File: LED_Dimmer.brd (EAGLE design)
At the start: 48.3 x 62.2 mm, 12 parts

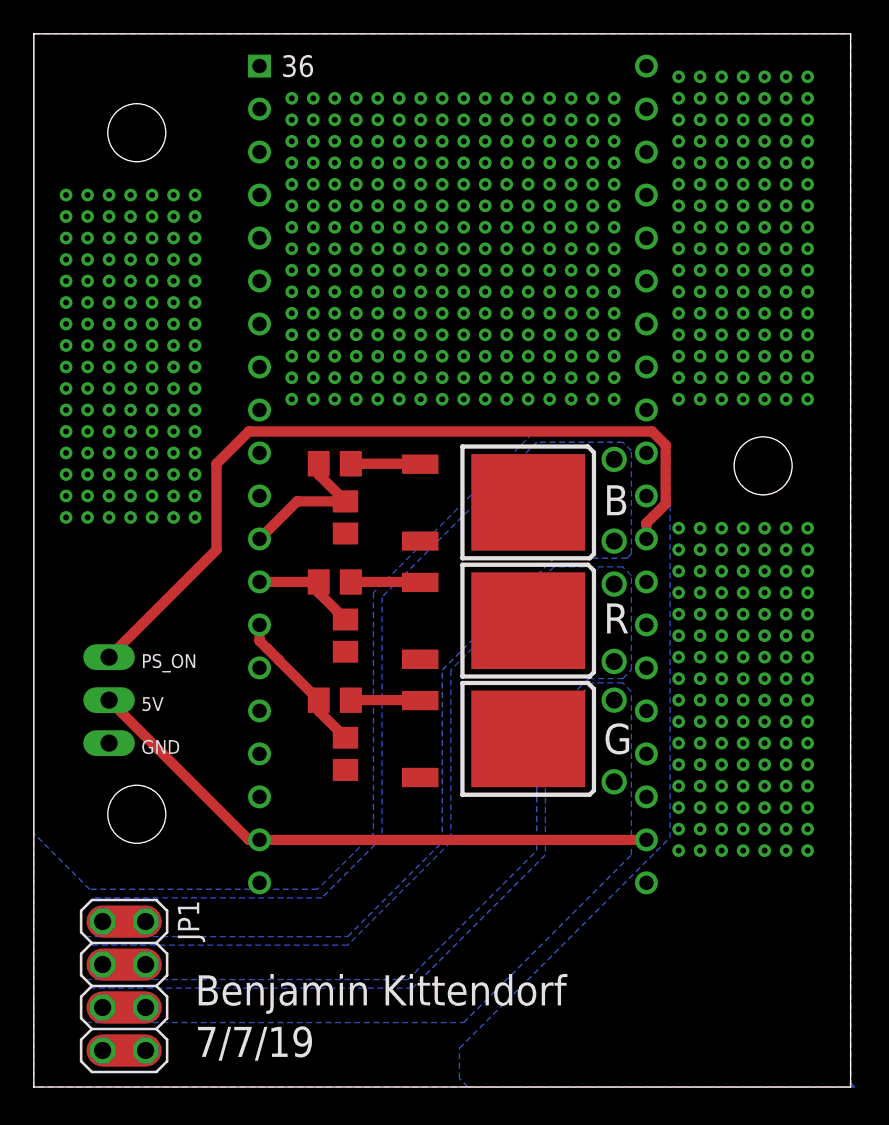
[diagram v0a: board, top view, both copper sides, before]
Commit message: retraced paths and edited clearances
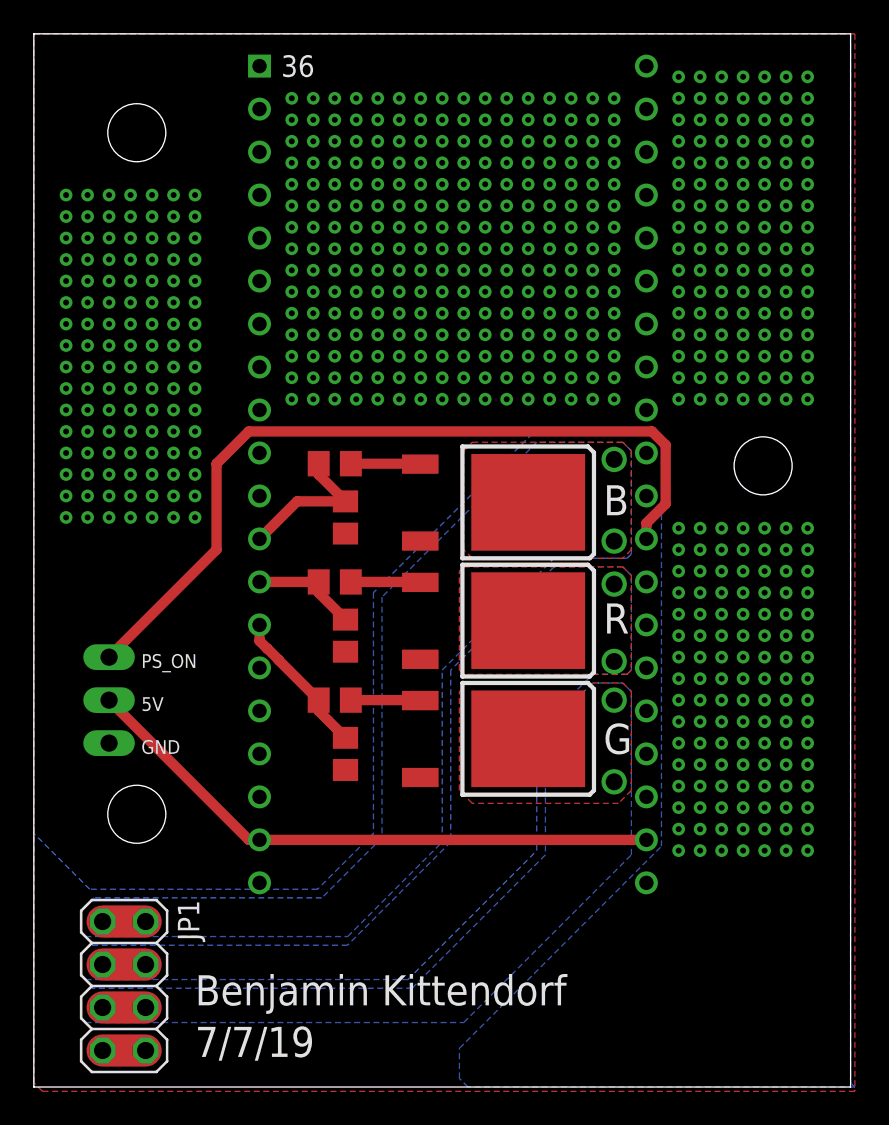
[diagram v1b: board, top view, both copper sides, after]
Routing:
- net N$6: vias 1 -> 2
- added copper zone on layer 1, net N$4
- added copper zone on layer 1, net N$6
- added copper zone on layer 1, net N$7
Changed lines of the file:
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@@
 <grid distance="10" unitdist="mil" unit="mil" style="lines" multiple="1" display="no" altdistance="5" altunitdist="mil" altunit="mil"/>
 <layers>
-<layer number="1" name="Top" color="4" fill="1" visible="yes" active="yes"/>
+<layer number="1" name="Top" color="4" fill="1" visible="no" active="yes"/>
 <layer number="2" name="Route2" color="16" fill="1" visible="no" active="no"/>
 <layer number="3" name="Route3" color="17" fill="1" visible="no" active="no"/>
@@
 <layer number="25" name="tNames" color="7" fill="1" visible="yes" active="yes"/>
 <layer number="26" name="bNames" color="7" fill="1" visible="yes" active="yes"/>
-<layer number="27" name="tValues" color="7" fill="1" visible="yes" active="yes"/>
-<layer number="28" name="bValues" color="7" fill="1" visible="yes" active="yes"/>
-<layer number="29" name="tStop" color="7" fill="3" visible="yes" active="yes"/>
+<layer number="27" name="tValues" color="7" fill="1" visible="no" active="yes"/>
+<layer number="28" name="bValues" color="7" fill="1" visible="no" active="yes"/>
+<layer number="29" name="tStop" color="7" fill="3" visible="no" active="yes"/>
 <layer number="30" name="bStop" color="7" fill="6" visible="no" active="yes"/>
-<layer number="31" name="tCream" color="7" fill="4" visible="yes" active="yes"/>
-<layer number="32" name="bCream" color="7" fill="5" visible="yes" active="yes"/>
+<layer number="31" name="tCream" color="7" fill="4" visible="no" active="yes"/>
+<layer number="32" name="bCream" color="7" fill="5" visible="no" active="yes"/>
 <layer number="33" name="tFinish" color="6" fill="3" visible="no" active="yes"/>
 <layer number="34" name="bFinish" color="6" fill="6" visible="no" active="yes"/>
@@
 <layer number="37" name="tTest" color="7" fill="1" visible="no" active="yes"/>
 <layer number="38" name="bTest" color="7" fill="1" visible="no" active="yes"/>
-<layer number="39" name="tKeepout" color="4" fill="11" visible="yes" active="yes"/>
+<layer number="39" name="tKeepout" color="4" fill="11" visible="no" active="yes"/>
 <layer number="40" name="bKeepout" color="1" fill="11" visible="no" active="yes"/>
 <layer number="41" name="tRestrict" color="4" fill="10" visible="no" active="yes"/>
 <layer number="42" name="bRestrict" color="1" fill="10" visible="no" active="yes"/>
 <layer number="43" name="vRestrict" color="2" fill="10" visible="no" active="yes"/>
-<layer number="44" name="Drills" color="7" fill="1" visible="yes" active="yes"/>
+<layer number="44" name="Drills" color="7" fill="1" visible="no" active="yes"/>
 <layer number="45" name="Holes" color="7" fill="1" visible="yes" active="yes"/>
 <layer number="46" name="Milling" color="3" fill="1" visible="no" active="yes"/>
 <layer number="47" name="Measures" color="7" fill="1" visible="no" active="yes"/>
 <layer number="48" name="Document" color="7" fill="1" visible="yes" active="yes"/>
-<layer number="49" name="Reference" color="7" fill="1" visible="yes" active="yes"/>
-<layer number="51" name="tDocu" color="7" fill="1" visible="yes" active="yes"/>
+<layer number="49" name="Reference" color="7" fill="1" visible="no" active="yes"/>
+<layer number="51" name="tDocu" color="7" fill="1" visible="no" active="yes"/>
 <layer number="52" name="bDocu" color="7" fill="1" visible="no" active="yes"/>
 <layer number="88" name="SimResults" color="9" fill="1" visible="no" active="no"/>
@@
 <via x="34.29" y="23.368" extent="1-16" drill="1"/>
 <via x="34.29" y="28.194" extent="1-16" drill="1"/>
-<polygon width="0.1524" layer="16">
+<polygon width="0.1524" layer="16" thermals="no">
 <vertex x="3.556" y="2.286"/>
 <vertex x="2.794" y="1.524"/>
@@
 <vertex x="17.018" y="2.286"/>
 </polygon>
-<wire x1="34.29" y1="23.368" x2="29.21" y2="25.654" width="0" layer="19" extent="1-1"/>
+<polygon width="0.127" layer="1" thermals="no">
+<vertex x="34.798" y="29.21"/>
+<vertex x="35.306" y="28.702"/>
+<vertex x="35.306" y="22.86"/>
+<vertex x="34.798" y="22.352"/>
+<vertex x="25.908" y="22.352"/>
+<vertex x="25.4" y="22.86"/>
+<vertex x="25.4" y="28.702"/>
+<vertex x="25.908" y="29.21"/>
+</polygon>
 </signal>
 <signal name="N$6">
@@
 <contactref element="FETG" pad="2"/>
 <via x="34.29" y="9.144" extent="1-16" drill="1"/>
-<polygon width="0.1524" layer="16">
+<polygon width="0.1524" layer="16" thermals="no">
 <vertex x="22.352" y="-3.048"/>
 <vertex x="3.302" y="-3.048"/>
@@
 <vertex x="30.226" y="4.826"/>
 </polygon>
-<wire x1="34.29" y1="9.144" x2="29.21" y2="11.684" width="0" layer="19" extent="1-1"/>
+<polygon width="0.127" layer="1" thermals="no">
+<vertex x="25.654" y="14.986"/>
+<vertex x="34.798" y="14.986"/>
+<vertex x="35.306" y="14.478"/>
+<vertex x="35.306" y="8.636"/>
+<vertex x="34.544" y="7.874"/>
+<vertex x="25.908" y="7.874"/>
+<vertex x="25.146" y="8.636"/>
+<vertex x="25.146" y="14.478"/>
+</polygon>
+<via x="34.29" y="13.97" extent="1-16" drill="1"/>
 </signal>
 <signal name="5V">
@@
 <contactref element="R6" pad="1"/>
 <contactref element="R4" pad="1"/>
-<polygon width="0.0762" layer="1">
-<vertex x="0" y="53.34"/>
-<vertex x="48.26" y="53.34"/>
-<vertex x="48.26" y="-8.89"/>
-<vertex x="0" y="-8.89"/>
-</polygon>
 <contactref element="FETR" pad="3"/>
 <contactref element="FETB" pad="3"/>
 <contactref element="FETG" pad="3"/>
-<polygon width="0.1524" layer="16">
+<polygon width="0.1524" layer="16" thermals="no">
 <vertex x="0" y="53.34"/>
 <vertex x="48.26" y="53.34"/>
@@
 <vertex x="25.146" y="-8.382"/>
 <vertex x="25.146" y="-6.604"/>
-<vertex x="37.592" y="5.842"/>
-<vertex x="37.592" y="28.702"/>
+<vertex x="37.084" y="5.334"/>
+<vertex x="37.084" y="29.21"/>
 <vertex x="36.576" y="29.718"/>
 <vertex x="29.464" y="29.718"/>
@@
 <vertex x="3.302" y="2.794"/>
 <vertex x="0" y="6.096"/>
+</polygon>
+<polygon width="0.127" layer="1" thermals="no" rank="2">
+<vertex x="0" y="53.34"/>
+<vertex x="48.514" y="53.34"/>
+<vertex x="48.514" y="-9.144"/>
+<vertex x="0.508" y="-9.144"/>
+<vertex x="0" y="-8.636"/>
 </polygon>
 </signal>
@@
 <via x="34.29" y="16.256" extent="1-16" drill="1"/>
 <via x="34.29" y="20.828" extent="1-16" drill="1"/>
-<polygon width="0.1524" layer="16">
+<polygon width="0.1524" layer="16" thermals="no">
 <vertex x="3.302" y="-0.508"/>
 <vertex x="2.794" y="-1.016"/>
@@
 <vertex x="29.718" y="5.08"/>
 <vertex x="29.718" y="12.192"/>
-<vertex x="32.766" y="15.24"/>
-<vertex x="34.798" y="15.24"/>
+<vertex x="33.02" y="15.494"/>
+<vertex x="35.052" y="15.494"/>
 <vertex x="35.306" y="15.748"/>
 <vertex x="35.306" y="21.336"/>
@@
 <vertex x="18.542" y="-0.508"/>
 </polygon>
-<wire x1="34.29" y1="20.828" x2="29.21" y2="18.669" width="0" layer="19" extent="1-1"/>
-</signal>
-<signal name="N6">
-<via x="34.29" y="13.97" extent="1-16" drill="1"/>
+<polygon width="0.127" layer="1" thermals="no">
+<vertex x="34.798" y="21.844"/>
+<vertex x="35.306" y="21.336"/>
+<vertex x="35.306" y="15.748"/>
+<vertex x="35.052" y="15.494"/>
+<vertex x="25.4" y="15.494"/>
+<vertex x="25.146" y="15.748"/>
+<vertex x="25.146" y="21.59"/>
+<vertex x="25.4" y="21.844"/>
+</polygon>
 </signal>
 </signals>
